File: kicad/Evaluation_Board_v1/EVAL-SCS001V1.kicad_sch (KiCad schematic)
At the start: 27 parts, among them J1 Screw_Terminal_01x02, J2 GSB1C211110DS1HR, U1 STL6P3LLH6, U2 STUSB4500QTR

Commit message: Edits to make sure I'm pushing correctly
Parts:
- removed J2: GSB1C211110DS1HR, GSB1C211110DS1HR:AMPHENOL_GSB1C211110DS1HR, symbol GSB1C211110DS1HR:GSB1C211110DS1HR
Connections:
- net VBUS_A: no longer names the net of C50.1, CR3.1, R1.1, R10.1, TP1.1, U1.1 (S), U1.2 (S), U1.3 (S), U2.24 (VDD)

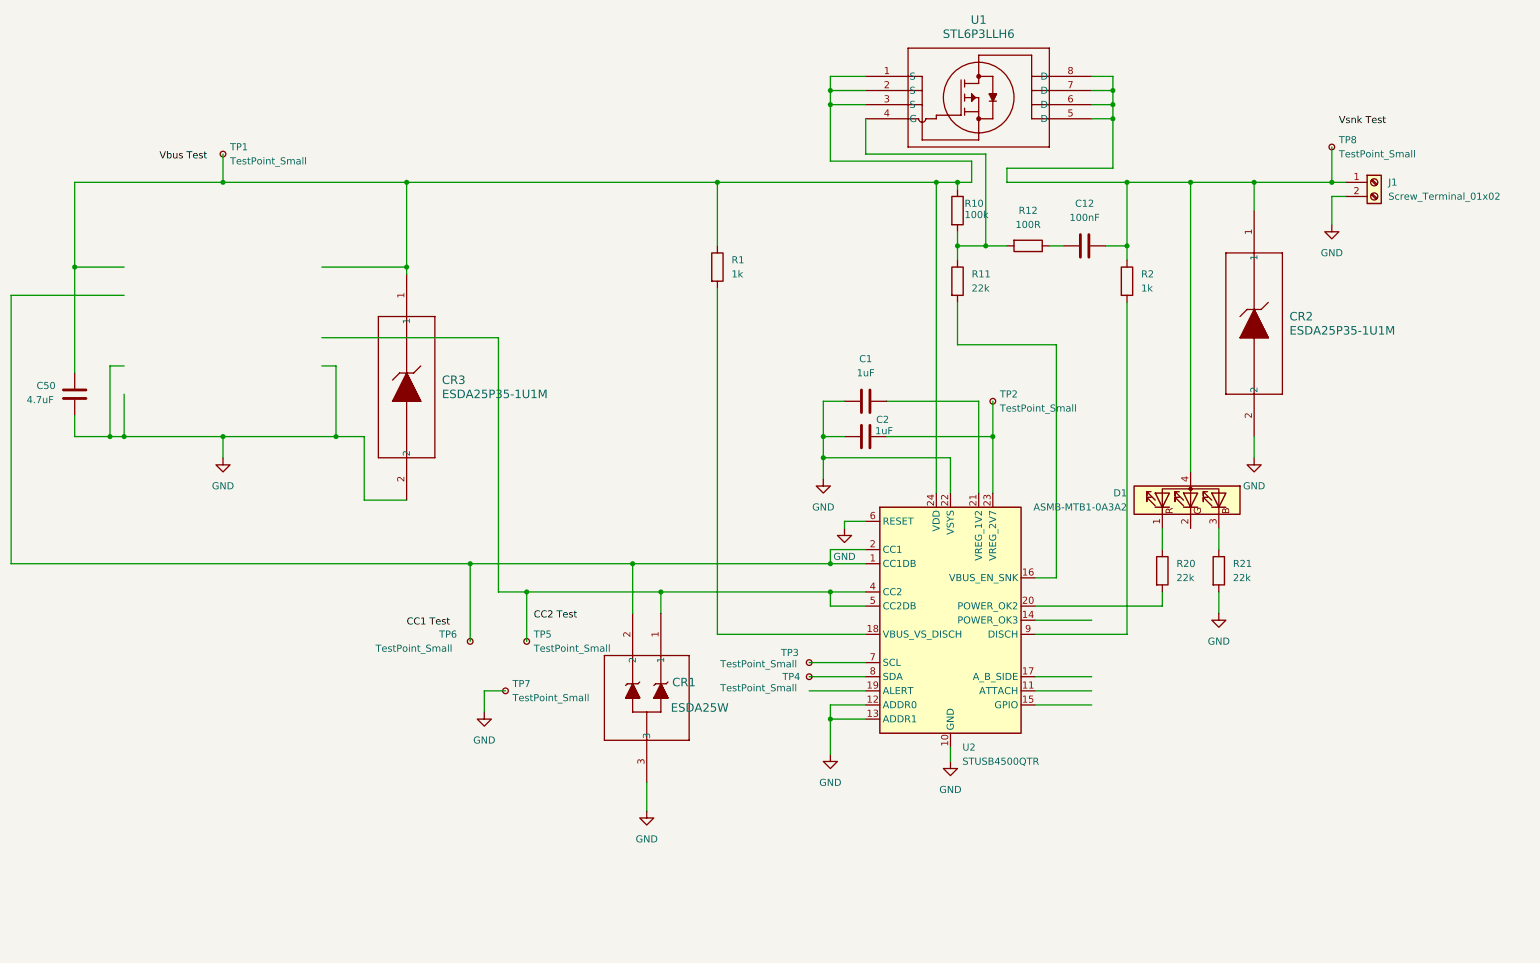
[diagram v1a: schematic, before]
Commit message: Updated schematic, still need to change symbols
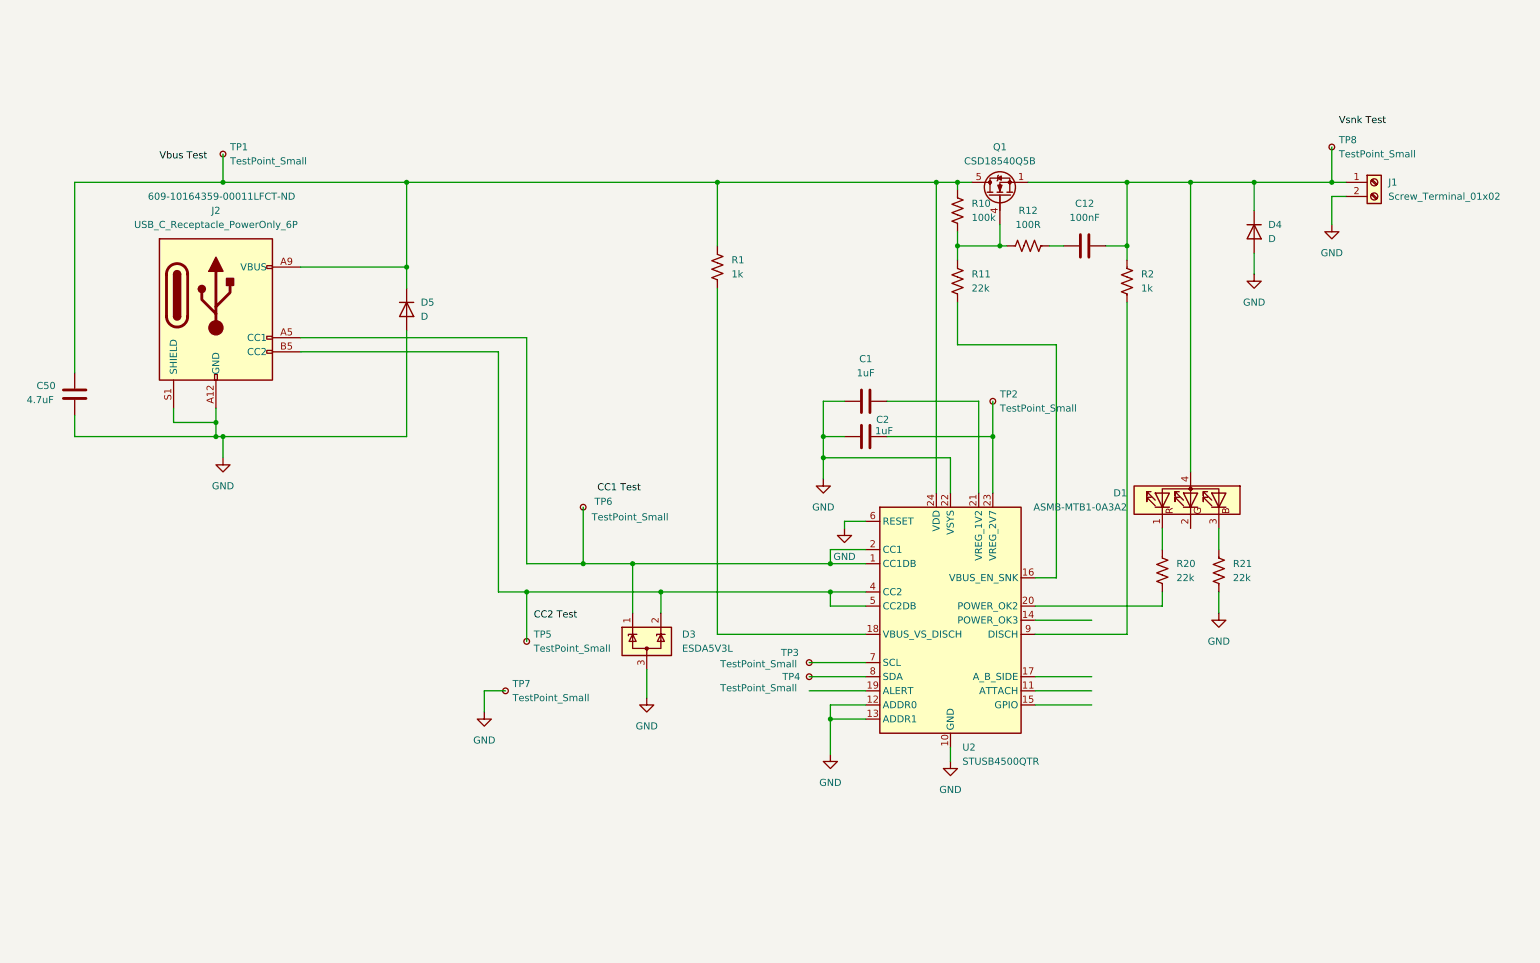
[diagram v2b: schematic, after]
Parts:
- removed CR1: ESDA25W, SOT323-3L_STM, symbol ESDA25W:ESDA25W
- removed CR2, CR3: ESDA25P35-1U1M, QFN1610_STM, symbol ESDA25P35:ESDA25P35-1U1M
- removed R1, R2: 1k, symbol Device:R
- removed R10: 100k, symbol Device:R
- removed R11, R20, R21: 22k, symbol Device:R
- removed R12: 100R, symbol Device:R
- removed U1: STL6P3LLH6, POWERFLAT_3P3X3P3_STM, symbol STL6P3LLH6:STL6P3LLH6
- added D3: ESDA5V3L, Package_TO_SOT_SMD:SOT-23-3, symbol Power_Protection:ESDA5V3L
- added D4, D5: D, symbol Device:D
- added J2: USB_C_Receptacle_PowerOnly_6P, my_USB:Amp_10164359_USB_Power, symbol Connector:USB_C_Receptacle_PowerOnly_6P
- added Q1: CSD18540Q5B, Package_TO_SOT_SMD:TDSON-8-1, symbol Transistor_FET:CSD18540Q5B
- added R1, R2: 1k, symbol Device:R_US
- added R10: 100k, symbol Device:R_US
- added R11, R20, R21: 22k, symbol Device:R_US
- added R12: 100R, symbol Device:R_US
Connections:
- net GND: now also D3.3 (A), D4.2 (A), D5.2 (A), J2.A12 (GND), J2.B12 (GND), J2.S1 (SHIELD), R21.2
- net at C50.1, TP1.1, U2.24 (VDD): now also D5.1 (K), J2.A9 (VBUS), J2.B9 (VBUS), Q1.5 (D), R1.1, R10.1
- net at C12.1, D1.4 (A), J1.1 (Pin_1)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: now also D4.1 (K), Q1.1 (S), Q1.2 (S), Q1.3 (S), R2.1
- net at TP5.1, U2.4 (CC2), U2.5 (CC2DB): now also D3.2 (K), J2.B5 (CC2)
- net at TP6.1, U2.1 (CC1DB), U2.2 (CC1): now also D3.1 (K), J2.A5 (CC1)
- net at D1.1 (RK): now also R20.1
- net at U2.20 (POWER_OK2): now also R20.2
- net at U2.16 (VBUS_EN_SNK): now also R11.2
- net at U2.18 (VBUS_VS_DISCH): now also R1.2
- net at C12.2: now also R12.2
- net at D1.3 (BK): now also R21.1
- net at U2.9 (DISCH): now also R2.2
- new net: Q1.4 (G), R10.2, R11.1, R12.1
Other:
- moved on the sheet: TP6

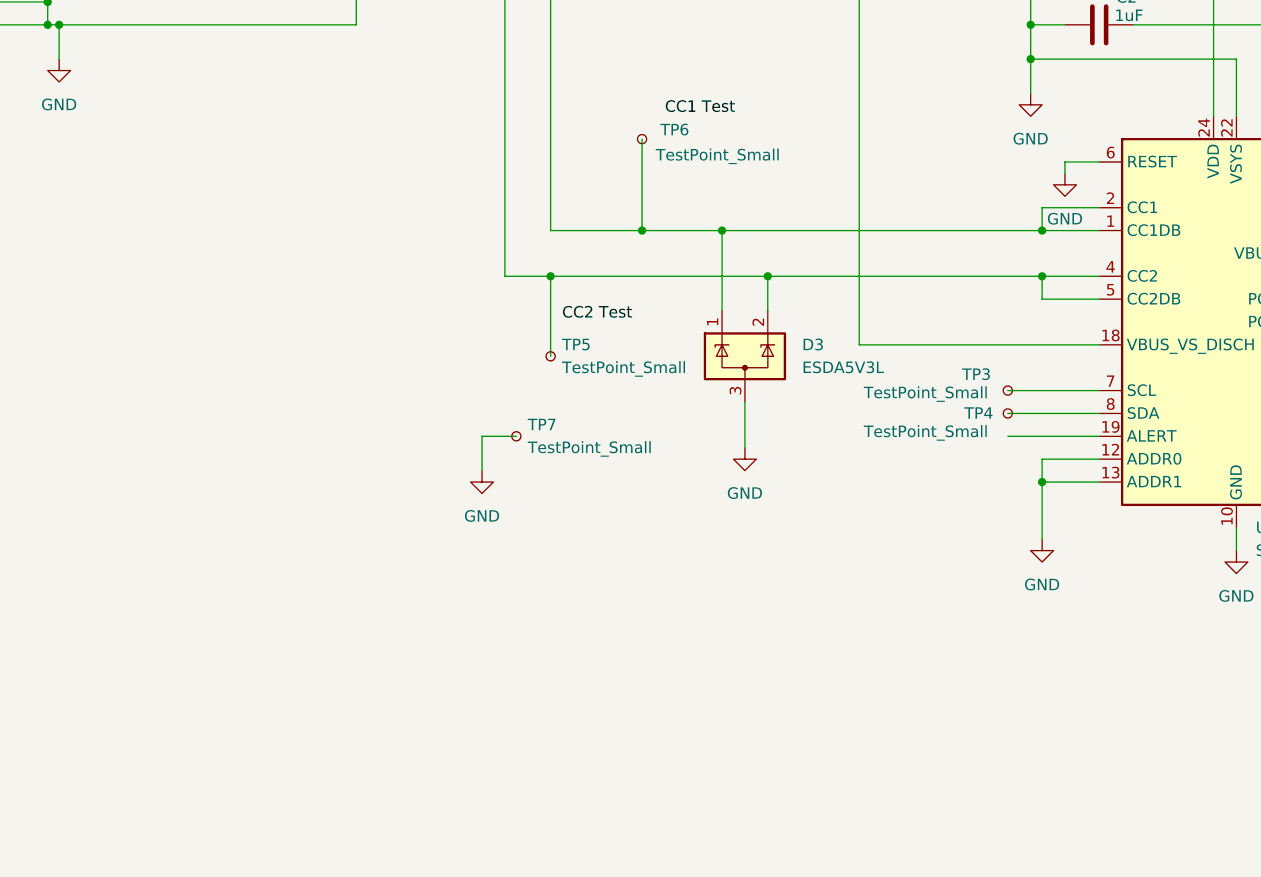
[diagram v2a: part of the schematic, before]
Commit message: Uploaded library (incorrectly?) and upadted schematic with arduino nano symbol
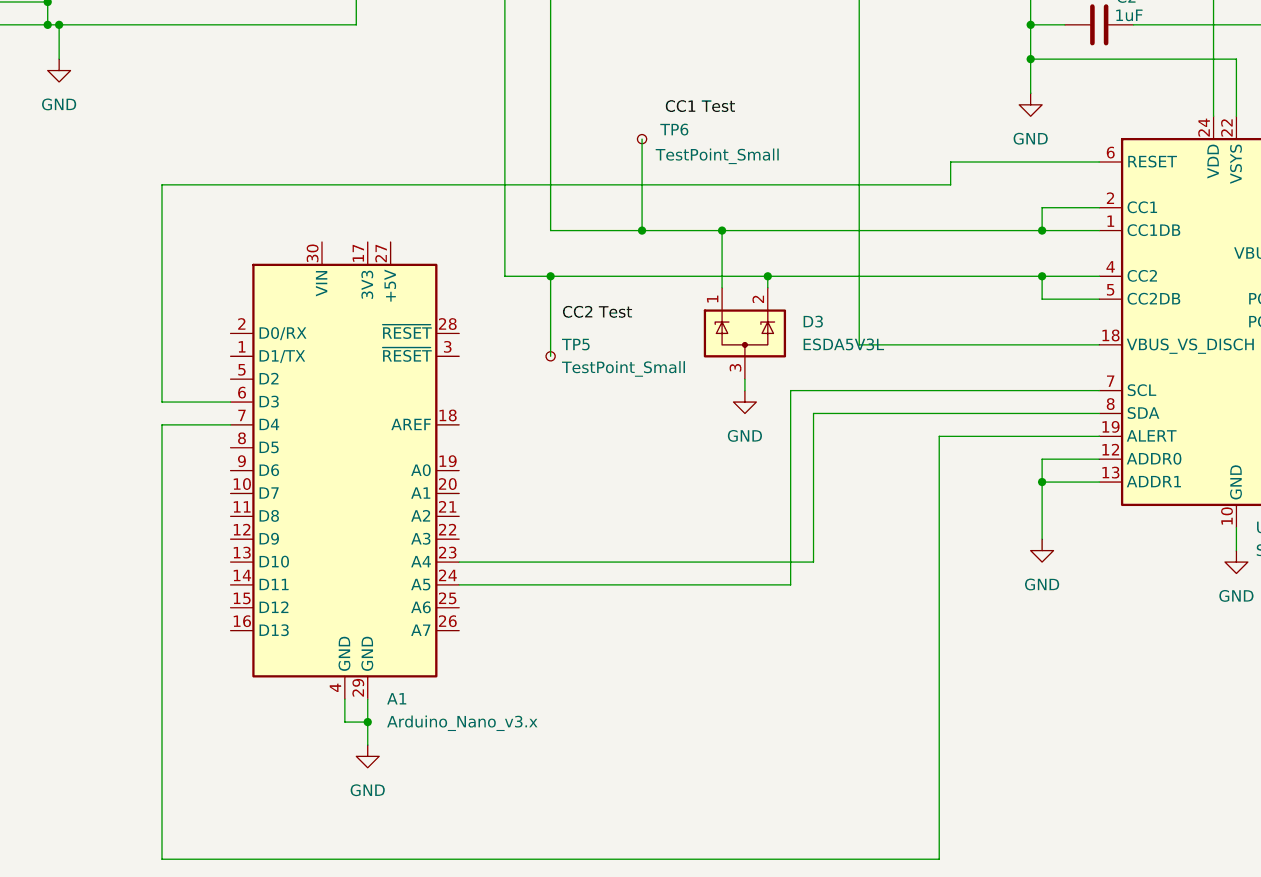
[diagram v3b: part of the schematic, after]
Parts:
- removed TP3, TP4, TP7: TestPoint_Small, symbol Connector:TestPoint_Small
- added A1: Arduino_Nano_v3.x, Module:Arduino_Nano, symbol MCU_Module:Arduino_Nano_v3.x
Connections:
- net GND: now also A1.29 (GND), A1.4 (GND); no longer U2.6 (RESET)
- net at U2.7 (SCL): now also A1.24 (A5)
- net at U2.19 (ALERT): now also A1.7 (D4)
- net at U2.8 (SDA): now also A1.23 (A4)
- new net: A1.6 (D3), U2.6 (RESET)
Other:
- moved on the sheet: D3

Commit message: Updated schematic with some footprints, still working on footprints before moving to PCB
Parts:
- C1: footprint (none) -> Capacitor_SMD:C_0603_1608Metric
- C12, C2, C50: footprint (none) -> Capacitor_SMD:C_0603_1608Metric_Pad1.08x0.95mm_HandSolder
- R1, R10, R11, R12, R2, R20, R21: footprint (none) -> Resistor_SMD:R_0603_1608Metric
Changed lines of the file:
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@@
 	)
 	(label "Vsnk Test"
-		(at 256.54 38.1 0)
+		(at 256.54 39.37 0)
 		(effects
 			(font
@@
 			)
 		)
-		(property "Footprint" ""
+		(property "Footprint" "Resistor_SMD:R_0603_1608Metric"
 			(at 145.796 63.754 90)
 			(hide yes)
@@
 			)
 		)
-		(property "Footprint" ""
+		(property "Footprint" "Capacitor_SMD:C_0603_1608Metric_Pad1.08x0.95mm_HandSolder"
 			(at 207.01 60.6552 0)
 			(hide yes)
@@
 			)
 		)
-		(property "Footprint" ""
+		(property "Footprint" "Resistor_SMD:R_0603_1608Metric"
 			(at 188.976 66.294 90)
 			(hide yes)
@@
 			)
 		)
-		(property "Footprint" ""
+		(property "Footprint" "Resistor_SMD:R_0603_1608Metric"
 			(at 235.966 118.364 90)
 			(hide yes)
@@
 			)
 		)
-		(property "Footprint" ""
+		(property "Footprint" "Resistor_SMD:R_0603_1608Metric"
 			(at 225.806 118.364 90)
 			(hide yes)
@@
 			)
 		)
-		(property "Footprint" ""
+		(property "Footprint" "Resistor_SMD:R_0603_1608Metric"
 			(at 200.914 58.674 90)
 			(hide yes)
@@
 			)
 		)
-		(property "Footprint" ""
+		(property "Footprint" "Capacitor_SMD:C_0603_1608Metric_Pad1.08x0.95mm_HandSolder"
 			(at 175.26 93.0148 0)
 			(hide yes)
@@
 			)
 		)
-		(property "Footprint" ""
+		(property "Footprint" "Capacitor_SMD:C_0603_1608Metric"
 			(at 175.26 86.6648 0)
 			(hide yes)
@@
 			)
 		)
-		(property "Footprint" ""
+		(property "Footprint" "Capacitor_SMD:C_0603_1608Metric_Pad1.08x0.95mm_HandSolder"
 			(at 30.1752 90.17 0)
 			(hide yes)
@@
 			)
 		)
-		(property "Footprint" ""
+		(property "Footprint" "Resistor_SMD:R_0603_1608Metric"
 			(at 188.976 53.594 90)
 			(hide yes)
@@
 			)
 		)
-		(property "Footprint" ""
+		(property "Footprint" "Resistor_SMD:R_0603_1608Metric"
 			(at 219.456 66.294 90)
 			(hide yes)

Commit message: Update EVAL-SCS001V1.kicad_sch
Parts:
- C1: footprint Capacitor_SMD:C_0603_1608Metric -> Capacitor_SMD:C_0603_1608Metric_Pad1.08x0.95mm_HandSolder
- D4, D5: footprint (none) -> Diode_SMD:D_SOD-323
- J1: footprint (none) -> TerminalBlock_CUI:TerminalBlock_CUI_TB007-508-02_1x02_P5.08mm_Horizontal
- R1, R10, R11, R12, R2, R20, R21: footprint Resistor_SMD:R_0603_1608Metric -> Resistor_SMD:R_0603_1608Metric_Pad0.98x0.95mm_HandSolder
- TP1, TP2, TP5, TP6, TP8: footprint (none) -> TestPoint:TestPoint_Pad_D2.0mm
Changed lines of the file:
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@@
 			)
 		)
-		(property "Footprint" ""
+		(property "Footprint" "Diode_SMD:D_SOD-323"
 			(at 241.3 57.15 0)
 			(hide yes)
@@
 			)
 		)
-		(property "Footprint" ""
+		(property "Footprint" "TestPoint:TestPoint_Pad_D2.0mm"
 			(at 260.35 41.91 0)
 			(hide yes)
@@
 			)
 		)
-		(property "Footprint" ""
+		(property "Footprint" "TestPoint:TestPoint_Pad_D2.0mm"
 			(at 60.96 43.18 0)
 			(hide yes)
@@
 			)
 		)
-		(property "Footprint" "Resistor_SMD:R_0603_1608Metric"
+		(property "Footprint" "Resistor_SMD:R_0603_1608Metric_Pad0.98x0.95mm_HandSolder"
 			(at 145.796 63.754 90)
 			(hide yes)
@@
 			)
 		)
-		(property "Footprint" ""
+		(property "Footprint" "TestPoint:TestPoint_Pad_D2.0mm"
 			(at 125.73 106.68 0)
 			(hide yes)
@@
 			)
 		)
-		(property "Footprint" ""
+		(property "Footprint" "TestPoint:TestPoint_Pad_D2.0mm"
 			(at 115.57 130.81 0)
 			(hide yes)
@@
 			)
 		)
-		(property "Footprint" "Resistor_SMD:R_0603_1608Metric"
+		(property "Footprint" "Resistor_SMD:R_0603_1608Metric_Pad0.98x0.95mm_HandSolder"
 			(at 188.976 66.294 90)
 			(hide yes)
@@
 			)
 		)
-		(property "Footprint" ""
+		(property "Footprint" "TestPoint:TestPoint_Pad_D2.0mm"
 			(at 199.39 87.63 0)
 			(hide yes)
@@
 			)
 		)
-		(property "Footprint" "Resistor_SMD:R_0603_1608Metric"
+		(property "Footprint" "Resistor_SMD:R_0603_1608Metric_Pad0.98x0.95mm_HandSolder"
 			(at 235.966 118.364 90)
 			(hide yes)
@@
 			)
 		)
-		(property "Footprint" ""
+		(property "Footprint" "TerminalBlock_CUI:TerminalBlock_CUI_TB007-508-02_1x02_P5.08mm_Horizontal"
 			(at 262.89 48.26 0)
 			(hide yes)
@@
 			)
 		)
-		(property "Footprint" "Resistor_SMD:R_0603_1608Metric"
+		(property "Footprint" "Resistor_SMD:R_0603_1608Metric_Pad0.98x0.95mm_HandSolder"
 			(at 225.806 118.364 90)
 			(hide yes)
@@
 			)
 		)
-		(property "Footprint" "Resistor_SMD:R_0603_1608Metric"
+		(property "Footprint" "Resistor_SMD:R_0603_1608Metric_Pad0.98x0.95mm_HandSolder"
 			(at 200.914 58.674 90)
 			(hide yes)
@@
 			)
 		)
-		(property "Footprint" "Capacitor_SMD:C_0603_1608Metric"
+		(property "Footprint" "Capacitor_SMD:C_0603_1608Metric_Pad1.08x0.95mm_HandSolder"
 			(at 175.26 86.6648 0)
 			(hide yes)
@@
 			)
 		)
-		(property "Footprint" ""
+		(property "Footprint" "Diode_SMD:D_SOD-323"
 			(at 88.9 71.12 0)
 			(hide yes)
@@
 			)
 		)
-		(property "Footprint" "Resistor_SMD:R_0603_1608Metric"
+		(property "Footprint" "Resistor_SMD:R_0603_1608Metric_Pad0.98x0.95mm_HandSolder"
 			(at 188.976 53.594 90)
 			(hide yes)
@@
 			)
 		)
-		(property "Footprint" "Resistor_SMD:R_0603_1608Metric"
+		(property "Footprint" "Resistor_SMD:R_0603_1608Metric_Pad0.98x0.95mm_HandSolder"
 			(at 219.456 66.294 90)
 			(hide yes)

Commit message: Worked on PCB, added footprints (still need to verify some)
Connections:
- net at C12.1, D1.4 (A), D4.1 (K)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: now also Q1.5 (S); no longer Q1.1 (S)
- net at C50.1, D5.1 (K), J2.A9 (VBUS)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: now also Q1.[1-3] (D); no longer Q1.5 (D)
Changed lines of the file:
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@@
 	(wire
 		(pts
-			(xy 201.93 142.24) (xy 212.09 142.24)
-		)
-		(stroke
-			(width 0)
-			(type default)
-		)
-	)
-	(wire
-		(pts
 			(xy 184.15 48.26) (xy 187.96 48.26)
 		)
@@
 	(wire
 		(pts
-			(xy 201.93 137.16) (xy 212.09 137.16)
-		)
-		(stroke
-			(width 0)
-			(type default)
-		)
-	)
-	(wire
-		(pts
 			(xy 218.44 62.23) (xy 218.44 59.69)
 		)
@@
 	(wire
 		(pts
-			(xy 201.93 139.7) (xy 212.09 139.7)
-		)
-		(stroke
-			(width 0)
-			(type default)
-		)
-	)
-	(wire
-		(pts
 			(xy 171.45 109.22) (xy 154.94 109.22)
 		)
@@
 	(wire
 		(pts
-			(xy 201.93 127) (xy 212.09 127)
-		)
-		(stroke
-			(width 0)
-			(type default)
-		)
-	)
-	(wire
-		(pts
 			(xy 201.93 119.38) (xy 205.74 119.38)
 		)
@@
 	)
 	(label "CC2 Test"
-		(at 111.76 127 0)
+		(at 111.76 128.27 0)
 		(effects
 			(font
@@
 	)
 	(label "Vbus Test"
-		(at 44.45 44.45 0)
+		(at 57.15 40.64 0)
 		(effects
 			(font
@@
 		(pin "2"
 		)
-		(pin "1"
+		(pin "[1-3]"
 		)
 		(pin "5"
@@
 		(in_pos_files yes)
 		(dnp no)
-		(fields_autoplaced yes)
 		(property "Reference" "D1"
-			(at 218.44 104.1399 90)
+			(at 243.84 103.886 90)
 			(show_name no)
 			(do_not_autoplace no)
@@
 		)
 		(property "Value" "ASMB-MTB1-0A3A2"
-			(at 218.44 106.6799 90)
+			(at 260.096 106.68 90)
 			(show_name no)
 			(do_not_autoplace no)
